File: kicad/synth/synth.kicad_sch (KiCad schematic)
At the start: 20 parts, among them J1 PWR_LED_HEADER, J2 Conn_02x04_Top_Bottom, J3 Conn_02x04_Top_Bottom, J4 Conn_02x04_Top_Bottom, J5 Conn_02x04_Top_Bottom, J6 AUDIO_OUT, J7 RESET_BTN_HEADER, J8 POWER_IN, J9 USB_A, U1 Pico

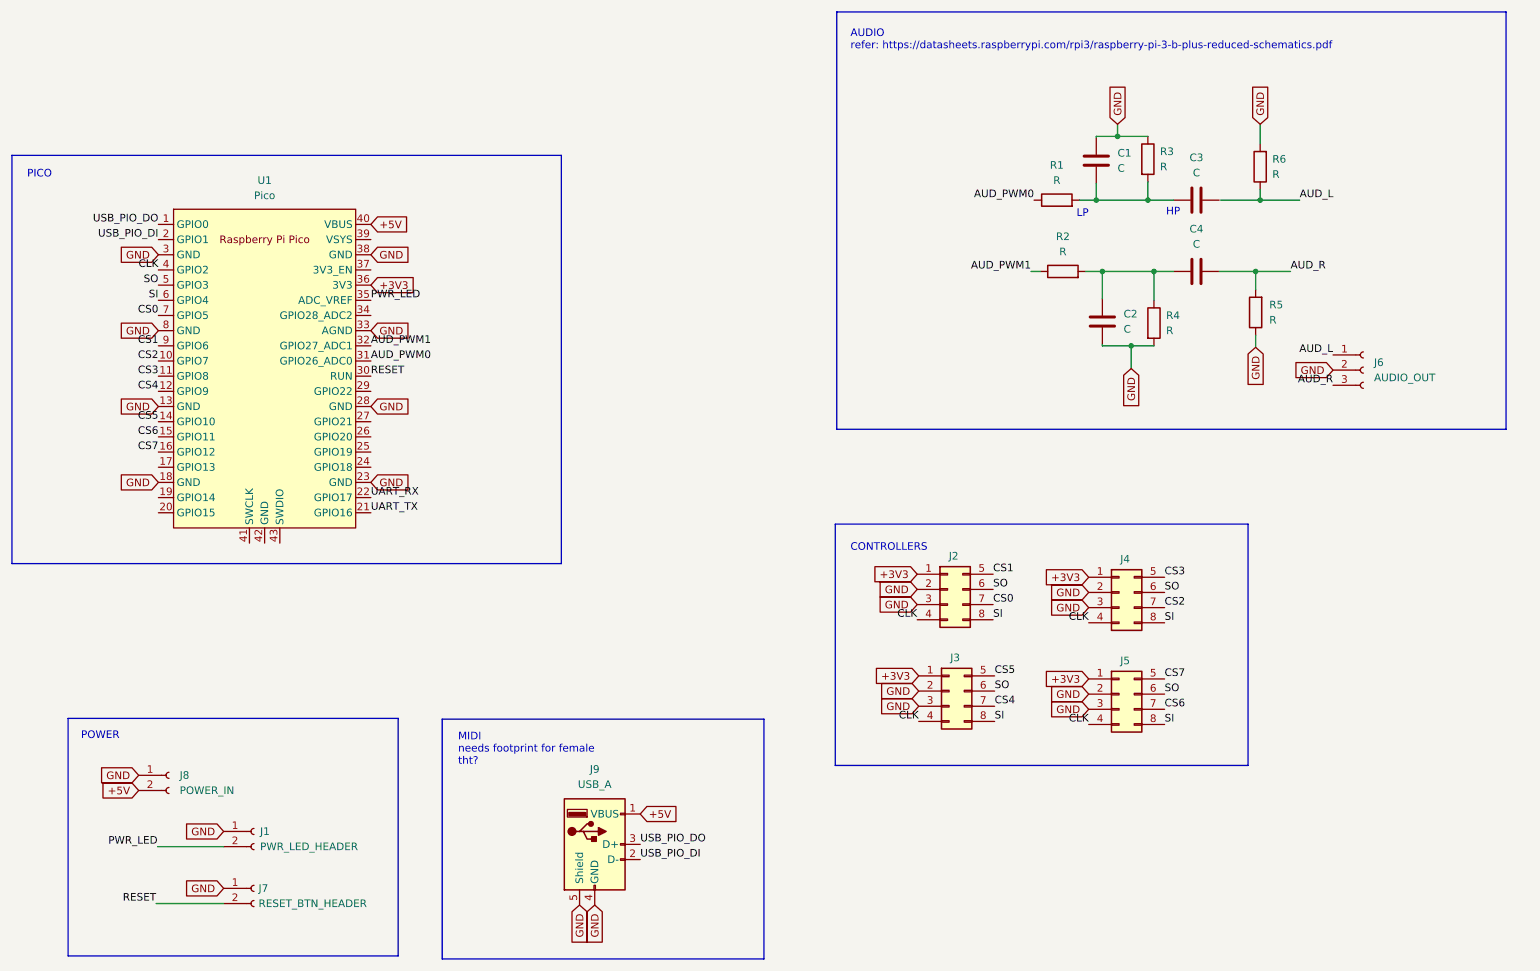
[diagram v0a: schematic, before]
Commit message: USB PIO now works and can control via PC or direct MIDI device :)
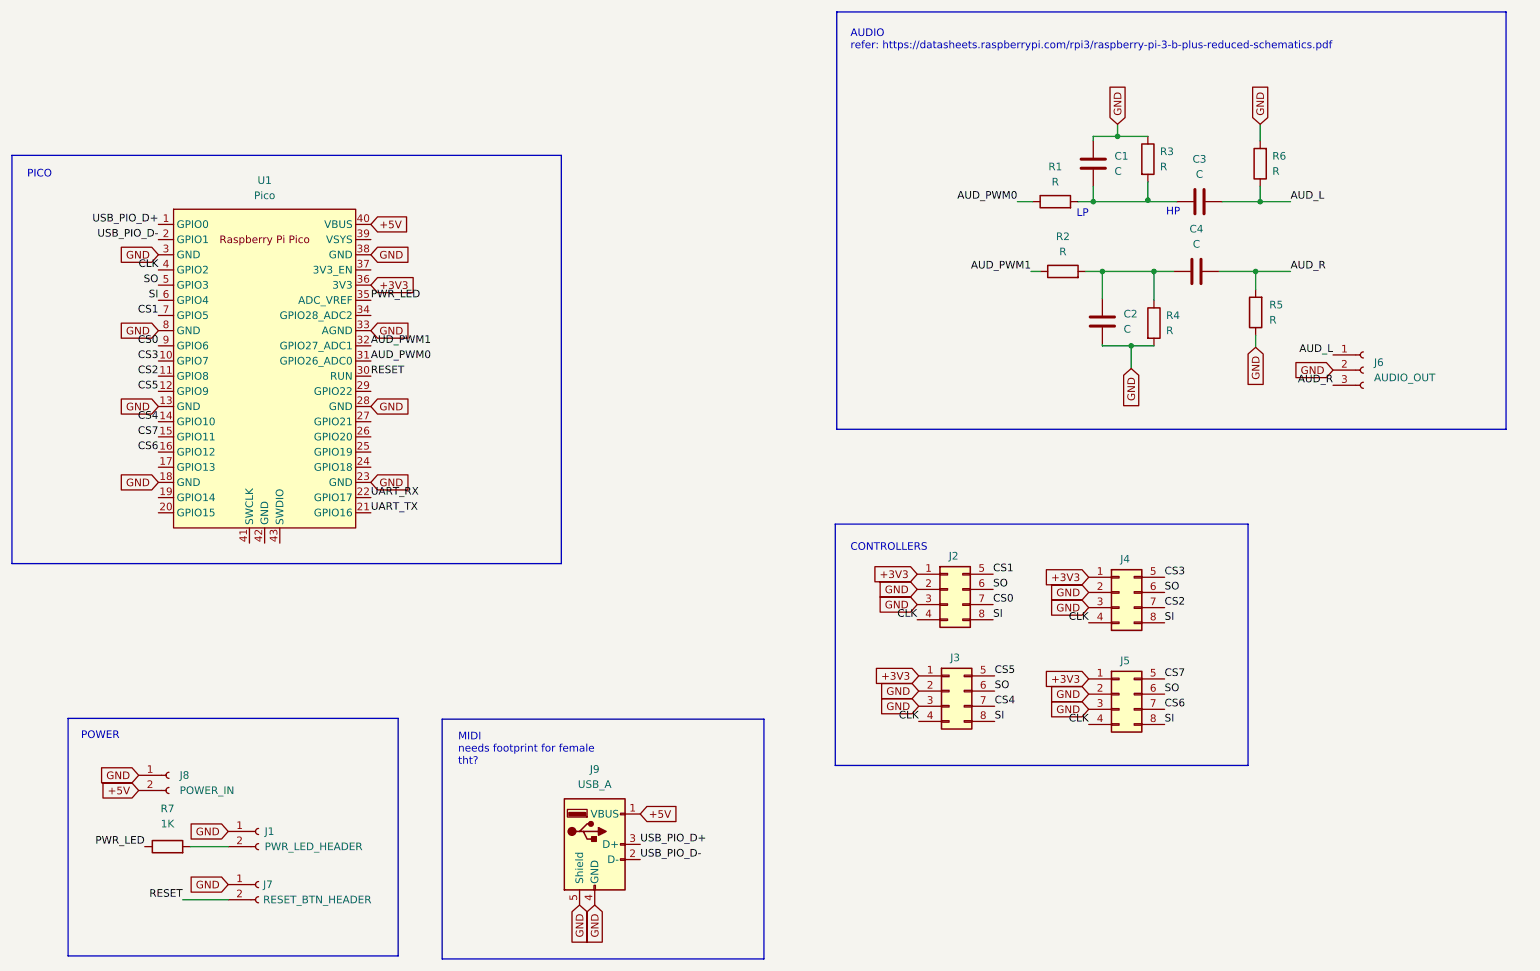
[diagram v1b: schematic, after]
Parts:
- added R7: 1K, Resistor_SMD:R_0805_2012Metric_Pad1.20x1.40mm_HandSolder, symbol Device:R
- J1, J7, J8: footprint Connector_PinHeader_1.00mm:PinHeader_1x02_P1.00mm_Vertical -> Connector_PinHeader_2.54mm:PinHeader_1x02_P2.54mm_Vertical
- J6: footprint Connector_PinHeader_1.00mm:PinHeader_1x03_P1.00mm_Vertical -> Connector_PinHeader_2.54mm:PinHeader_1x03_P2.54mm_Vertical
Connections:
- net AUD_L: now also C3.2
- net CS0: now also U1.9 (GPIO6); no longer U1.7 (GPIO5)
- net CS1: now also U1.7 (GPIO5); no longer U1.9 (GPIO6)
- net CS2: now also U1.11 (GPIO8); no longer U1.10 (GPIO7)
- net CS3: now also U1.10 (GPIO7); no longer U1.11 (GPIO8)
- net CS4: now also U1.14 (GPIO10); no longer U1.12 (GPIO9)
- net CS5: now also U1.12 (GPIO9); no longer U1.14 (GPIO10)
- net CS6: now also U1.16 (GPIO12); no longer U1.15 (GPIO11)
- net CS7: now also U1.15 (GPIO11); no longer U1.16 (GPIO12)
- net PWR_LED: now also R7.1; no longer J1.2 (Pin_2)
- net USB_PIO_DI renamed USB_PIO_D-
- net USB_PIO_DO renamed USB_PIO_D+
- new net: J1.2 (Pin_2), R7.2
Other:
- moved on the sheet: C1, C3, J1, J7, R6
